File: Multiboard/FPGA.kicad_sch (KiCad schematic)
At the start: 58 parts, among them J6 Conn_02x20_Odd_Even, J7 Conn_02x20_Odd_Even, J8 USB_C_Receptacle_USB2.0_16P, U10 USBLC6-2SC6, U6 LCMXO2-1200ZE-1TG144C, U7 FAN1112, U8 NCP1117

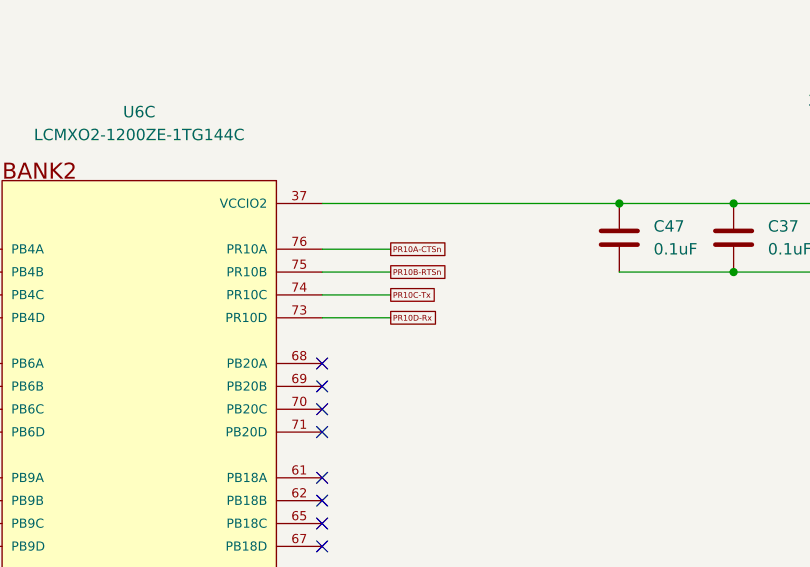
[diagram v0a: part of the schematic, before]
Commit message: Fixed trace angle
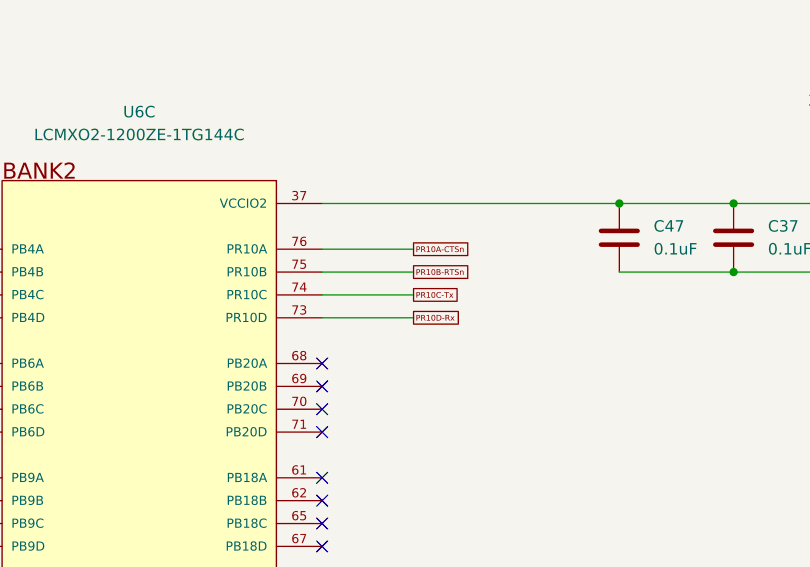
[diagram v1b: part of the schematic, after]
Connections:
- net at U6.15 (NC), U6.17 (NC), U6.31 (NC)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: no longer U6.103 (NC), U6.129 (NC), U6.89 (NC)
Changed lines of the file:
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@@
 	(wire
 		(pts
-			(xy 345.44 138.43) (xy 353.06 138.43)
+			(xy 345.44 138.43) (xy 355.6 138.43)
 		)
 		(stroke
@@
 	(wire
 		(pts
-			(xy 345.44 140.97) (xy 353.06 140.97)
+			(xy 345.44 140.97) (xy 355.6 140.97)
 		)
 		(stroke
@@
 	(wire
 		(pts
-			(xy 345.44 143.51) (xy 353.06 143.51)
+			(xy 345.44 143.51) (xy 355.6 143.51)
 		)
 		(stroke
@@
 	(wire
 		(pts
-			(xy 345.44 135.89) (xy 353.06 135.89)
+			(xy 345.44 135.89) (xy 355.6 135.89)
 		)
 		(stroke
@@
 	(global_label "PR10B-RTSn"
 		(shape passive)
-		(at 353.06 138.43 0)
+		(at 355.6 138.43 0)
 		(fields_autoplaced yes)
 		(effects
@@
 		)
 		(property "Intersheetrefs" "${INTERSHEET_REFS}"
-			(at 360.196 138.43 0)
+			(at 362.736 138.43 0)
 			(effects
 				(font
@@
 	(global_label "PR10D-Rx"
 		(shape passive)
-		(at 353.06 143.51 0)
+		(at 355.6 143.51 0)
 		(fields_autoplaced yes)
 		(effects
@@
 		)
 		(property "Intersheetrefs" "${INTERSHEET_REFS}"
-			(at 359.0469 143.51 0)
+			(at 361.5869 143.51 0)
 			(effects
 				(font
@@
 	(global_label "PR10C-Tx"
 		(shape passive)
-		(at 353.06 140.97 0)
+		(at 355.6 140.97 0)
 		(fields_autoplaced yes)
 		(effects
@@
 		)
 		(property "Intersheetrefs" "${INTERSHEET_REFS}"
-			(at 358.8957 140.97 0)
+			(at 361.4357 140.97 0)
 			(effects
 				(font
@@
 	(global_label "PR10A-CTSn"
 		(shape passive)
-		(at 353.06 135.89 0)
+		(at 355.6 135.89 0)
 		(fields_autoplaced yes)
 		(effects
@@
 		)
 		(property "Intersheetrefs" "${INTERSHEET_REFS}"
-			(at 360.1053 135.89 0)
+			(at 362.6453 135.89 0)
 			(effects
 				(font
@@
 		(pin "24"
 		)
-		(pin "89"
-		)
 		(pin "17"
 		)
@@
 		(pin "87"
 		)
-		(pin "103"
-		)
-		(pin "15"
-		)
 		(pin "31"
 		)
 		(pin "89"
 		)
-		(pin "129"
-		)
-		(pin "15-UB"
-		)
-		(pin "15-UC"
-		)
-		(pin "15-UD"
+		(pin "15"
 		)
 		(instances
@@
 		(pin "24"
 		)
-		(pin "103"
-		)
-		(pin "129"
-		)
-		(pin "15"
-		)
 		(pin "17"
 		)
@@
 		(pin "89"
 		)
-		(pin "15-UB"
-		)
-		(pin "15-UC"
-		)
-		(pin "15-UD"
-		)
-		(pin "89"
+		(pin "15"
 		)
 		(instances
@@
 		(pin "24"
 		)
-		(pin "15-UB"
-		)
-		(pin "15-UC"
-		)
-		(pin "89"
-		)
 		(pin "17"
 		)
-		(pin "15"
-		)
 		(pin "87"
 		)
@@
 		(pin "31"
 		)
-		(pin "103"
-		)
-		(pin "129"
-		)
-		(pin "15-UD"
+		(pin "15"
 		)
 		(instances
@@
 		(pin "24"
 		)
-		(pin "89"
-		)
 		(pin "17"
 		)
-		(pin "129"
-		)
 		(pin "89"
 		)
 		(pin "31"
 		)
-		(pin "15"
-		)
 		(pin "87"
 		)
-		(pin "103"
-		)
 		(pin "63"
 		)
-		(pin "15-UB"
-		)
-		(pin "15-UC"
-		)
-		(pin "15-UD"
+		(pin "15"
 		)
 		(instances

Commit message: Generated BOM
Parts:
- C34, C35, C36, C37, C38, C39, C40, C41, C42, C43, C44, C45, C46, C47, C52, C53: LCSC Part Number (none) -> C14663
- C48, C50, C55: LCSC Part Number (none) -> C19702
- C49, C51: LCSC Part Number (none) -> C86295
- C54: LCSC Part Number (none) -> C95843
- C56: LCSC Part Number (none) -> C100042
- D10, D11, D12, D13, D14, D15, D7, D8, D9: LCSC Part Number (none) -> C2994781
- J8: LCSC Part Number (none) -> C2988369
- L4, L5: LCSC Part Number (none) -> C20345
- R57, R58: LCSC Part Number (none) -> C114662
- R59, R60: LCSC Part Number (none) -> C2907044
- R61: LCSC Part Number (none) -> C105588
- R62, R64: LCSC Part Number (none) -> C95177
- R63, R65, R66, R67, R68, R69, R70, R71, R72: LCSC Part Number (none) -> C22548
- U10: LCSC Part Number (none) -> C7519
- U7: value FAN1112 -> AMS1117-1.2; LCSC Part Number (none) -> C14529
- U8: LCSC Part Number (none) -> C20546

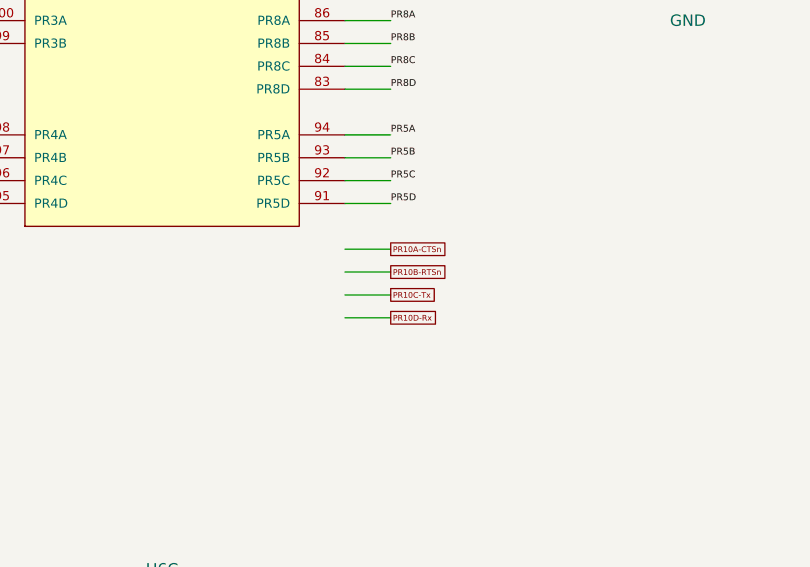
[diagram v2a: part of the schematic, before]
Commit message: fixed MCU LDO
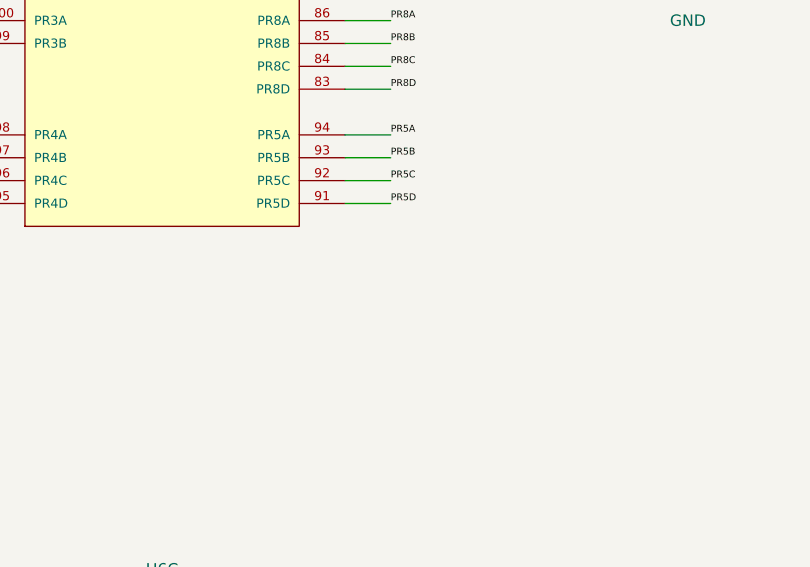
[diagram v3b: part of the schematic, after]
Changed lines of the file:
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@@
 	(wire
 		(pts
-			(xy 345.44 87.63) (xy 350.52 87.63)
-		)
-		(stroke
-			(width 0)
-			(type default)
-		)
-	)
-	(wire
-		(pts
 			(xy 67.31 46.99) (xy 82.55 46.99)
 		)
@@
 	(wire
 		(pts
-			(xy 345.44 90.17) (xy 350.52 90.17)
-		)
-		(stroke
-			(width 0)
-			(type default)
-		)
-	)
-	(wire
-		(pts
 			(xy 248.92 140.97) (xy 261.62 140.97)
 		)
@@
 	(wire
 		(pts
-			(xy 345.44 85.09) (xy 350.52 85.09)
-		)
-		(stroke
-			(width 0)
-			(type default)
-		)
-	)
-	(wire
-		(pts
 			(xy 251.46 218.44) (xy 251.46 222.25)
 		)
@@
 	(wire
 		(pts
-			(xy 345.44 92.71) (xy 350.52 92.71)
-		)
-		(stroke
-			(width 0)
-			(type default)
-		)
-	)
-	(wire
-		(pts
 			(xy 73.66 52.07) (xy 82.55 52.07)
 		)
@@
 		)
 	)
-	(global_label "PR10C-Tx"
-		(shape passive)
-		(at 350.52 90.17 0)
-		(fields_autoplaced yes)
-		(effects
-			(font
-				(size 0.635 0.635)
-			)
-			(justify left)
-		)
-		(property "Intersheetrefs" "${INTERSHEET_REFS}"
-			(at 356.3557 90.17 0)
-			(effects
-				(font
-					(size 1.27 1.27)
-				)
-				(justify left)
-				(hide yes)
-			)
-		)
-	)
 	(global_label "PR10A-CTSn"
 		(shape passive)
@@
 		)
 	)
-	(global_label "PR10A-CTSn"
-		(shape passive)
-		(at 350.52 85.09 0)
-		(fields_autoplaced yes)
-		(effects
-			(font
-				(size 0.635 0.635)
-			)
-			(justify left)
-		)
-		(property "Intersheetrefs" "${INTERSHEET_REFS}"
-			(at 357.5653 85.09 0)
-			(effects
-				(font
-					(size 1.27 1.27)
-				)
-				(justify left)
-				(hide yes)
-			)
-		)
-	)
-	(global_label "PR10D-Rx"
-		(shape passive)
-		(at 350.52 92.71 0)
-		(fields_autoplaced yes)
-		(effects
-			(font
-				(size 0.635 0.635)
-			)
-			(justify left)
-		)
-		(property "Intersheetrefs" "${INTERSHEET_REFS}"
-			(at 356.5069 92.71 0)
-			(effects
-				(font
-					(size 1.27 1.27)
-				)
-				(justify left)
-				(hide yes)
-			)
-		)
-	)
 	(global_label "PT10C-TDO"
 		(shape passive)
@@
 				(hide yes)
 			)
-		)
-	)
-	(global_label "PR10B-RTSn"
-		(shape passive)
-		(at 350.52 87.63 0)
-		(fields_autoplaced yes)
-		(effects
-			(font
-				(size 0.635 0.635)
-			)
-			(justify left)
-		)
-		(property "Intersheetrefs" "${INTERSHEET_REFS}"
-			(at 357.656 87.63 0)
-			(effects
-				(font
-					(size 1.27 1.27)
-				)
-				(justify left)
-				(hide yes)
-			)

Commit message: Restored older version due to KiCAD glitching
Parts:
- U7: LCSC Part Number C14529 -> (none)
- U8: LCSC Part Number C20546 -> ?C20546?
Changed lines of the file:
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@@
 			)
 		)
-		(property "LCSC Part Number" "C20546"
+		(property "LCSC Part Number" "?C20546?"
 			(at 77.47 204.47 0)
 			(effects
@@
 		(exclude_from_sim no)
 		(in_bom yes)
-		(on_board no)
+		(on_board yes)
 		(dnp no)
 		(fields_autoplaced yes)
@@
 			)
 		)
-		(property "LCSC Part Number" "C14529"
+		(property "LCSC Part Number" ""
 			(at 53.34 251.46 0)
 			(effects
@@
 		(exclude_from_sim no)
 		(in_bom yes)
-		(on_board no)
+		(on_board yes)
 		(dnp no)
 		(fields_autoplaced yes)
@@
 		(exclude_from_sim no)
 		(in_bom yes)
-		(on_board no)
+		(on_board yes)
 		(dnp no)
 		(fields_autoplaced yes)
@@
 		(exclude_from_sim no)
 		(in_bom yes)
-		(on_board no)
+		(on_board yes)
 		(dnp no)
 		(fields_autoplaced yes)

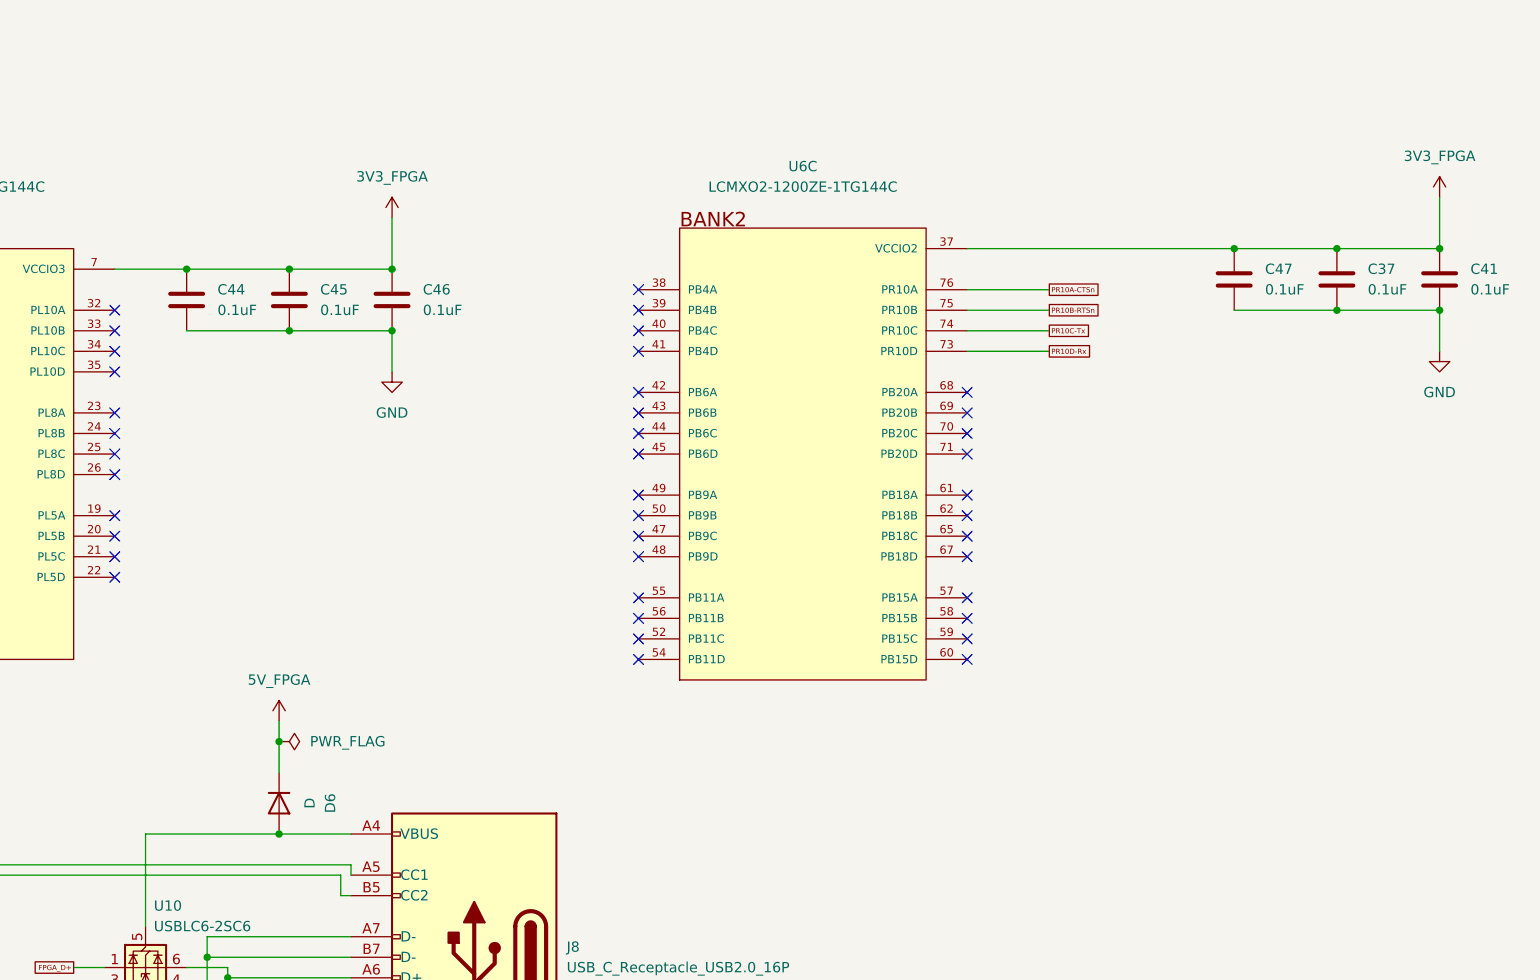
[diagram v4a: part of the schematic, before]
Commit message: Fixed glitched nets issue
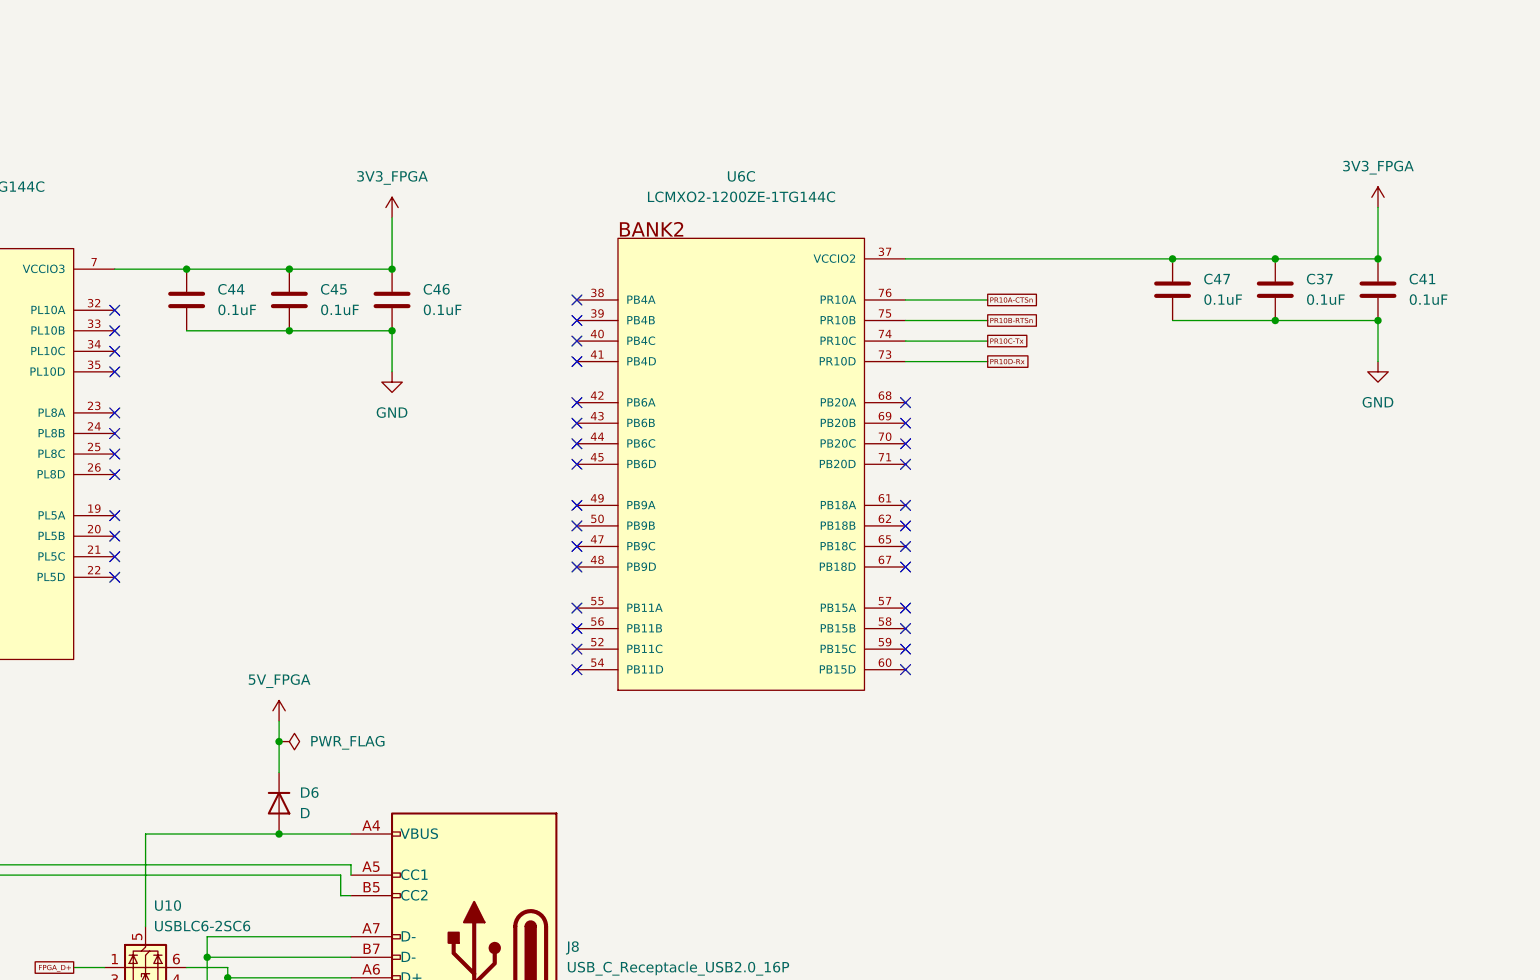
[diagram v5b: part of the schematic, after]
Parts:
- D6, J6, J7, U6: now left out of the parts list
- U7: LCSC Part Number (none) -> C14529
- U8: LCSC Part Number ?C20546? -> C20546
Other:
- moved on the sheet: C37, C41, C47, U6C
